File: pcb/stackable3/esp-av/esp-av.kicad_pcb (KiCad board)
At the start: 2 copper layers, 100 x 66 mm, 131 parts, among them J0 DC-005, J1 USB_C_Receptacle_USB2.0_16P, J10 JST SH, J11 STEMMA-Signal, J12 Qwiic, J13 Qwiic, J14 Pin socket, J15 Pin Socket, J16 Pin socket, J2 PJ-327U, J3 PJ-327U, J4 PJ-327U, J5 PJ-327U, J6 PJ-327U, J7 PJ-327U, J8 PJ-327U, J9 PJ-327U, Q1 PDNM6ET20V05, Q10 DMP1045U, Q11 DMP1045U, Q12 DMP1045U, Q13 DMP1045U, Q2 DMG6968U, Q3 DMP1045U, Q4 DMP1045U, Q5 DMP1045U, Q6 DMP1045U, Q7 PDNM6ET20V05, Q8 PDNM6ET20V05, Q9 PDNM6ET20V05, SW1 Reset, SW2 Boot, U1 USBLC6-2P6, U10 SN74LVC1T45Z6, U11 SN74LVC1T45Z6, U12 74HC595, U13 74HC595, U2 ME6211C33M5, U3 TPS563201, U4 NC7WZ14P6X, U5 NC7WZ14P6X, U6 SN74LVC1G157DC, U7 SN74LVC1G157DC, U8 SN74LVC1G157DC, U9 SN74LVC1G157DC

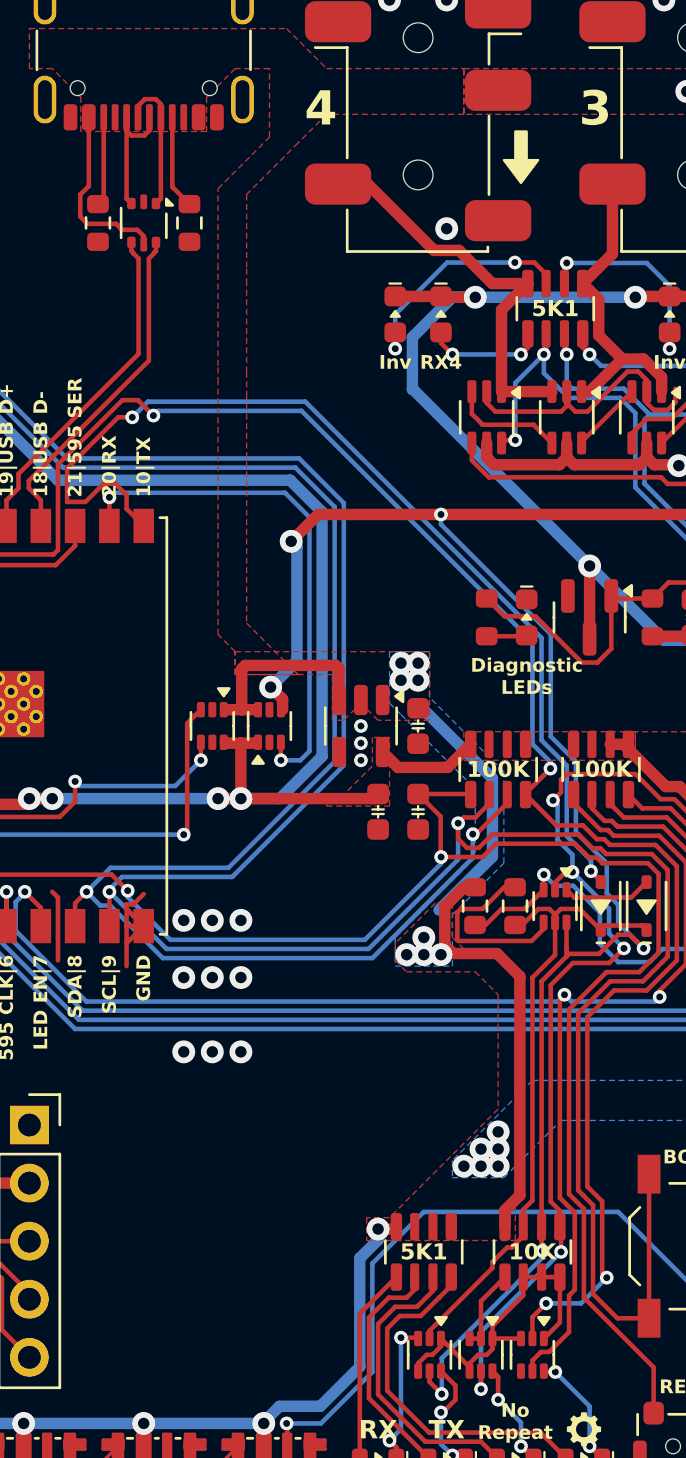
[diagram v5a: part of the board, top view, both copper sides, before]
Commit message: Add two more 5V power capacitors
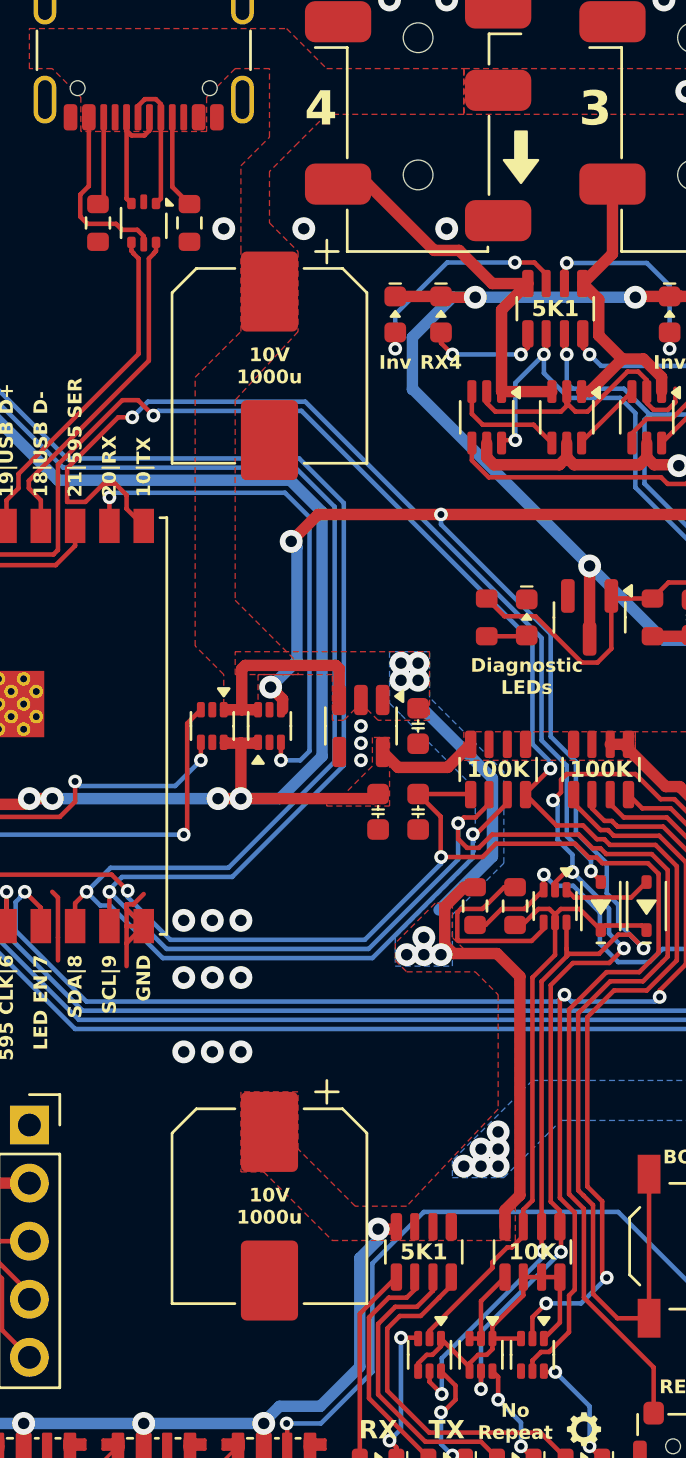
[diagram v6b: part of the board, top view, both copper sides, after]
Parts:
- added C7: 1000u, Capacitor_SMD:CP_Elec_8x10, F.Cu at (146.5, 71.2)
- added C8: 1000u, Capacitor_SMD:CP_Elec_8x10, F.Cu at (146.5, 108.0)
- renumbered C9 to C6
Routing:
- net GND: vias 49 -> 51

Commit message: Rearrange silkscreen title, logos
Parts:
- removed the REF** at (199.0, 96.0)
- added REF**: OSHW-Logo_7.5x8mm_SilkScreen, Symbol:OSHW-Logo_7.5x8mm_SilkScreen, F.Cu at (206.0, 96.0)
- moved G*** 7.00 mm to (199.0, 96.0)
